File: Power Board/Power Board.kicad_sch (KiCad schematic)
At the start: 0 parts

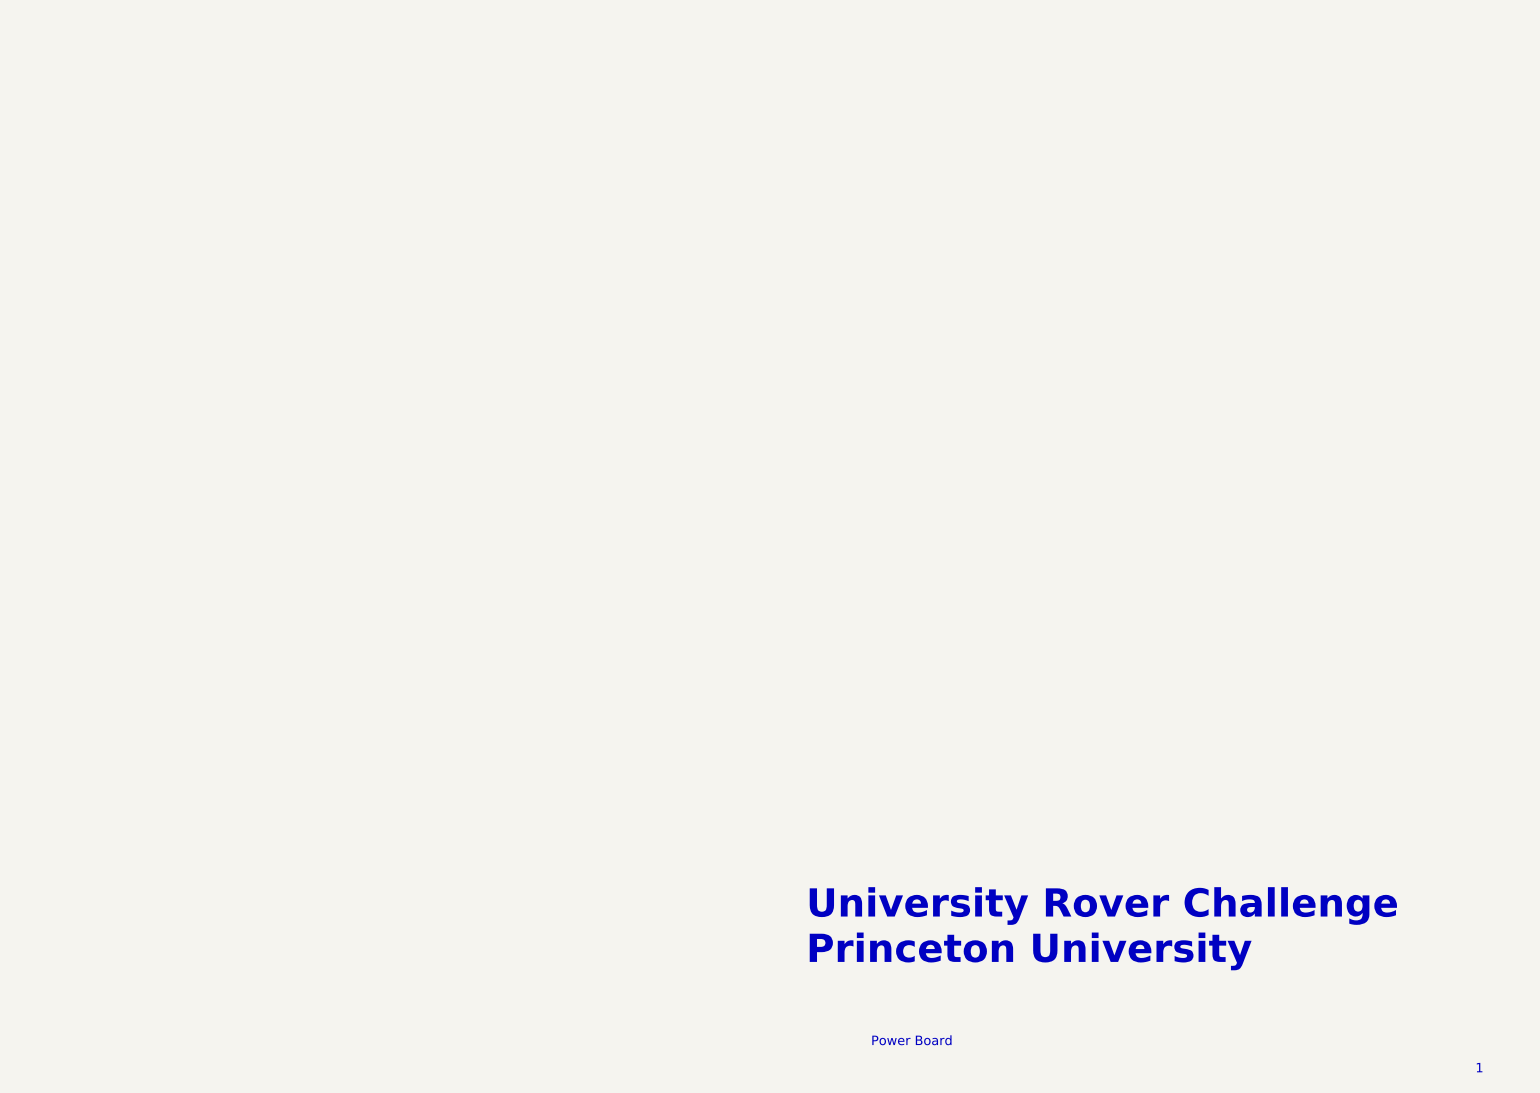
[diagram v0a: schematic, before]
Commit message: Updated power board schematic and libraries
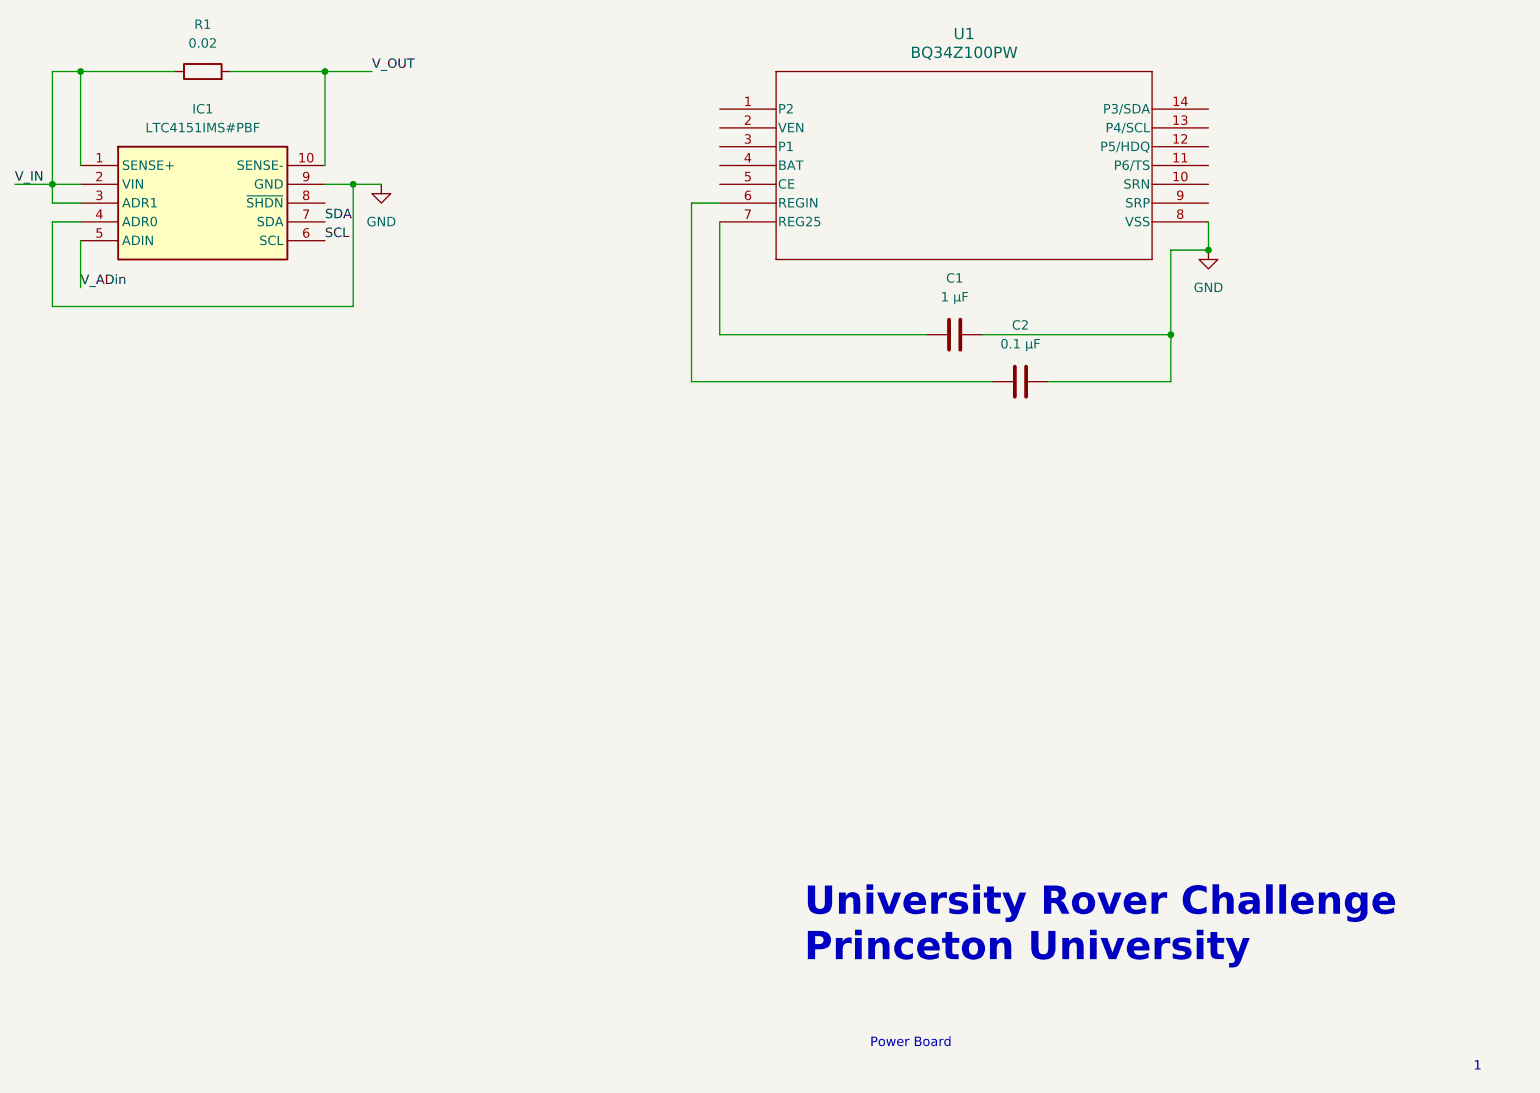
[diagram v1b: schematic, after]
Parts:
- added C1: 1 μF, symbol Device:C
- added C2: 0.1 μF, symbol Device:C
- added IC1: LTC4151IMS#PBF, SOP50P490X110-10N, symbol LTC4151IMS#PBF:LTC4151IMS#PBF
- added R1: 0.02, symbol Device:R
- added U1: BQ34Z100PW, PW14_TEX, symbol BQ34Z100PW:BQ34Z100PW
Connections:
- new net: C2.1, U1.6 (REGIN)
- new net: C1.1, U1.7 (REG25)
- new net GND: C1.2, C2.2, IC1.4 (ADR0), IC1.9 (GND), U1.8 (VSS)
- new net SCL: IC1.6 (SCL)
- new net SDA: IC1.7 (SDA)
- new net V_ADin: IC1.5 (ADIN)
- new net V_IN: IC1.1 (SENSE+), IC1.2 (VIN), IC1.3 (ADR1), R1.1
- new net V_OUT: IC1.10 (SENSE-), R1.2

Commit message: Worked on gas gauge
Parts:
- added R2, R3, R4: R, symbol Device:R
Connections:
- net GND: now also U1.1 (P2), U1.12 (P5/HDQ), U1.3 (P1)
- net SCL: now also U1.13 (P4/SCL)
- net SDA: now also U1.14 (P3/SDA)
- net PACK-: now reaches U1.10 (SRN)
- net PACK-: now also R2.1
- net at U1.4 (BAT): now also R3.2, R4.1
- net BAT-: now reaches U1.9 (SRP)
- net BAT-: now also R2.2
- new net BAT+: R3.1
- new net GNDA: R4.2
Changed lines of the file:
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@@
   (junction (at 76.2 73.66) (diameter 0) (color 0 0 0 0)
   )
+  (junction (at 232.41 78.74) (diameter 0) (color 0 0 0 0)
+  )
+  (junction (at 148.59 78.74) (diameter 0) (color 0 0 0 0)
+  )
+  (junction (at 160.02 63.5) (diameter 0) (color 0 0 0 0)
+  )
   (junction (at 116.84 73.66) (diameter 0) (color 0 0 0 0)
   )
   (junction (at 227.33 93.98) (diameter 0) (color 0 0 0 0)
   )
+  (junction (at 240.03 73.66) (diameter 0) (color 0 0 0 0)
+  )
   (junction (at 232.41 82.55) (diameter 0) (color 0 0 0 0)
   )
   (junction (at 113.03 58.42) (diameter 0) (color 0 0 0 0)
   )
+  (wire (pts (xy 80.01 58.42) (xy 92.71 58.42))
+    (stroke (width 0) (type default))
+  )
+  (wire (pts (xy 160.02 63.5) (xy 166.37 63.5))
+    (stroke (width 0) (type default))
+  )
+  (wire (pts (xy 233.68 81.28) (xy 240.03 81.28))
+    (stroke (width 0) (type default))
+  )
+  (wire (pts (xy 80.01 81.28) (xy 80.01 87.63))
+    (stroke (width 0) (type default))
+  )
+  (wire (pts (xy 233.68 81.28) (xy 233.68 76.2))
+    (stroke (width 0) (type default))
+  )
+  (wire (pts (xy 148.59 86.36) (xy 148.59 90.17))
+    (stroke (width 0) (type default))
+  )
+  (wire (pts (xy 237.49 68.58) (xy 237.49 78.74))
+    (stroke (width 0) (type default))
+  )
+  (wire (pts (xy 232.41 73.66) (xy 240.03 73.66))
+    (stroke (width 0) (type default))
+  )
+  (wire (pts (xy 240.03 73.66) (xy 248.92 73.66))
+    (stroke (width 0) (type default))
+  )
+  (wire (pts (xy 116.84 73.66) (xy 116.84 90.17))
+    (stroke (width 0) (type default))
+  )
+  (wire (pts (xy 227.33 82.55) (xy 232.41 82.55))
+    (stroke (width 0) (type default))
+  )
+  (wire (pts (xy 154.94 63.5) (xy 160.02 63.5))
+    (stroke (width 0) (type default))
+  )
+  (wire (pts (xy 76.2 78.74) (xy 76.2 90.17))
+    (stroke (width 0) (type default))
+  )
+  (wire (pts (xy 227.33 93.98) (xy 227.33 82.55))
+    (stroke (width 0) (type default))
+  )
+  (wire (pts (xy 142.24 69.85) (xy 148.59 69.85))
+    (stroke (width 0) (type default))
+  )
+  (wire (pts (xy 166.37 76.2) (xy 162.56 76.2))
+    (stroke (width 0) (type default))
+  )
+  (wire (pts (xy 113.03 58.42) (xy 119.38 58.42))
+    (stroke (width 0) (type default))
+  )
+  (wire (pts (xy 232.41 63.5) (xy 241.3 63.5))
+    (stroke (width 0) (type default))
+  )
   (wire (pts (xy 232.41 78.74) (xy 232.41 82.55))
     (stroke (width 0) (type default))
   )
-  (wire (pts (xy 80.01 58.42) (xy 92.71 58.42))
-    (stroke (width 0) (type default))
-  )
-  (wire (pts (xy 80.01 81.28) (xy 80.01 87.63))
-    (stroke (width 0) (type default))
-  )
-  (wire (pts (xy 116.84 73.66) (xy 116.84 90.17))
-    (stroke (width 0) (type default))
-  )
-  (wire (pts (xy 227.33 82.55) (xy 232.41 82.55))
-    (stroke (width 0) (type default))
-  )
-  (wire (pts (xy 76.2 78.74) (xy 76.2 90.17))
-    (stroke (width 0) (type default))
-  )
-  (wire (pts (xy 227.33 93.98) (xy 227.33 82.55))
-    (stroke (width 0) (type default))
-  )
-  (wire (pts (xy 166.37 76.2) (xy 162.56 76.2))
-    (stroke (width 0) (type default))
-  )
-  (wire (pts (xy 113.03 58.42) (xy 119.38 58.42))
-    (stroke (width 0) (type default))
-  )
   (wire (pts (xy 210.82 100.33) (xy 227.33 100.33))
     (stroke (width 0) (type default))
@@
     (stroke (width 0) (type default))
   )
+  (wire (pts (xy 148.59 83.82) (xy 148.59 78.74))
+    (stroke (width 0) (type default))
+  )
+  (wire (pts (xy 156.21 78.74) (xy 148.59 78.74))
+    (stroke (width 0) (type default))
+  )
+  (wire (pts (xy 233.68 76.2) (xy 232.41 76.2))
+    (stroke (width 0) (type default))
+  )
+  (wire (pts (xy 148.59 77.47) (xy 148.59 78.74))
+    (stroke (width 0) (type default))
+  )
   (wire (pts (xy 76.2 73.66) (xy 76.2 58.42))
     (stroke (width 0) (type default))
   )
+  (wire (pts (xy 166.37 71.12) (xy 156.21 71.12))
+    (stroke (width 0) (type default))
+  )
+  (wire (pts (xy 232.41 66.04) (xy 241.3 66.04))
+    (stroke (width 0) (type default))
+  )
   (wire (pts (xy 227.33 100.33) (xy 227.33 93.98))
     (stroke (width 0) (type default))
@@
     (stroke (width 0) (type default))
   )
+  (wire (pts (xy 166.37 68.58) (xy 160.02 68.58))
+    (stroke (width 0) (type default))
+  )
   (wire (pts (xy 162.56 76.2) (xy 162.56 100.33))
     (stroke (width 0) (type default))
   )
+  (wire (pts (xy 160.02 68.58) (xy 160.02 63.5))
+    (stroke (width 0) (type default))
+  )
   (wire (pts (xy 80.01 78.74) (xy 76.2 78.74))
     (stroke (width 0) (type default))
   )
+  (wire (pts (xy 156.21 71.12) (xy 156.21 78.74))
+    (stroke (width 0) (type default))
+  )
   (wire (pts (xy 76.2 90.17) (xy 116.84 90.17))
+    (stroke (width 0) (type default))
+  )
+  (wire (pts (xy 232.41 68.58) (xy 237.49 68.58))
+    (stroke (width 0) (type default))
+  )
+  (wire (pts (xy 237.49 78.74) (xy 232.41 78.74))
     (stroke (width 0) (type default))
   )
@@
     (effects (font (size 1.27 1.27)) (justify left bottom))
   )
+  (label "SDA" (at 234.95 63.5 0) (fields_autoplaced)
+    (effects (font (size 1.27 1.27)) (justify left bottom))
+  )
+  (label "SCL" (at 234.95 66.04 0) (fields_autoplaced)
+    (effects (font (size 1.27 1.27)) (justify left bottom))
+  )
   (label "V_OUT" (at 119.38 58.42 0) (fields_autoplaced)
     (effects (font (size 1.27 1.27)) (justify left bottom))
   )
+  (label "BAT-" (at 233.68 81.28 0) (fields_autoplaced)
+    (effects (font (size 1.27 1.27)) (justify left bottom))
+  )
   (label "V_ADin" (at 80.01 87.63 0) (fields_autoplaced)
     (effects (font (size 1.27 1.27)) (justify left bottom))
   )
+  (label "BAT+" (at 143.51 69.85 0) (fields_autoplaced)
+    (effects (font (size 1.27 1.27)) (justify left bottom))
+  )
+  (label "PACK-" (at 242.57 73.66 0) (fields_autoplaced)
+    (effects (font (size 1.27 1.27)) (justify left bottom))
+  )
   (label "SDA" (at 113.03 78.74 0) (fields_autoplaced)
     (effects (font (size 1.27 1.27)) (justify left bottom))
@@
   (label "V_IN" (at 71.12 73.66 0) (fields_autoplaced)
     (effects (font (size 1.27 1.27)) (justify left bottom))
+  )
+  (symbol (lib_id "power:GND") (at 154.94 63.5 0) (unit 1)
+    (in_bom yes) (on_board yes) (dnp no) (fields_autoplaced)
+    (property "Reference" "#PWR03" (at 154.94 69.85 0)
+      (effects (font (size 1.27 1.27)) hide)
+    )
+    (property "Value" "GND" (at 154.94 68.58 0)
+      (effects (font (size 1.27 1.27)))
+    )
+    (property "Footprint" "" (at 154.94 63.5 0)
+      (effects (font (size 1.27 1.27)) hide)
+    )
+    (property "Datasheet" "" (at 154.94 63.5 0)
+      (effects (font (size 1.27 1.27)) hide)
+    )
+    (pin "1")
+    (instances
+      (project "Power Board"
+        (path "/52f7cba9-f573-43e9-b6c5-44859a4c1733"
+          (reference "#PWR03") (unit 1)
+        )
+      )
+    )
+  )
+  (symbol (lib_id "power:GNDA") (at 148.59 90.17 0) (unit 1)
+    (in_bom yes) (on_board yes) (dnp no) (fields_autoplaced)
+    (property "Reference" "#PWR04" (at 148.59 96.52 0)
+      (effects (font (size 1.27 1.27)) hide)
+    )
+    (property "Value" "GNDA" (at 148.59 95.25 0)
+      (effects (font (size 1.27 1.27)))
+    )
+    (property "Footprint" "" (at 148.59 90.17 0)
+      (effects (font (size 1.27 1.27)) hide)
+    )
+    (property "Datasheet" "" (at 148.59 90.17 0)
+      (effects (font (size 1.27 1.27)) hide)
+    )
+    (pin "1")
+    (instances
+      (project "Power Board"
+        (path "/52f7cba9-f573-43e9-b6c5-44859a4c1733"
+          (reference "#PWR04") (unit 1)
+        )
+      )
+    )
   )
   (symbol (lib_id "BQ34Z100PW:BQ34Z100PW") (at 166.37 63.5 0) (unit 1)
@@
         )
       )
+    )
+  )
+  (symbol (lib_id "Device:R") (at 148.59 82.55 0) (unit 1)
+    (in_bom yes) (on_board yes) (dnp no) (fields_autoplaced)
+    (property "Reference" "R4" (at 151.13 81.28 0)
+      (effects (font (size 1.27 1.27)) (justify left))
+    )
+    (property "Value" "R" (at 151.13 83.82 0)
+      (effects (font (size 1.27 1.27)) (justify left))
+    )
+    (property "Footprint" "" (at 146.812 82.55 90)
+      (effects (font (size 1.27 1.27)) hide)
+    )
+    (property "Datasheet" "~" (at 148.59 82.55 0)
+      (effects (font (size 1.27 1.27)) hide)
+    )
+    (pin "1")
+    (pin "2")
+    (instances
+      (project "Power Board"
+        (path "/52f7cba9-f573-43e9-b6c5-44859a4c1733"
+          (reference "R4") (unit 1)
+        )
+      )
+    )
+  )
+  (symbol (lib_id "Device:R") (at 148.59 73.66 0) (unit 1)
+    (in_bom yes) (on_board yes) (dnp no) (fields_autoplaced)
+    (property "Reference" "R3" (at 151.13 72.39 0)
+      (effects (font (size 1.27 1.27)) (justify left))
+    )
+    (property "Value" "R" (at 151.13 74.93 0)
+      (effects (font (size 1.27 1.27)) (justify left))
+    )
+    (property "Footprint" "" (at 146.812 73.66 90)
+      (effects (font (size 1.27 1.27)) hide)
+    )
+    (property "Datasheet" "~" (at 148.59 73.66 0)
+      (effects (font (size 1.27 1.27)) hide)
+    )
+    (pin "1")
+    (pin "2")
+    (instances
+      (project "Power Board"
+        (path "/52f7cba9-f573-43e9-b6c5-44859a4c1733"
+          (reference "R3") (unit 1)
+        )
+      )
+    )
+  )
+  (symbol (lib_id "Device:R") (at 240.03 77.47 0) (unit 1)
+    (in_bom yes) (on_board yes) (dnp no) (fields_autoplaced)
+    (property "Reference" "R2" (at 242.57 76.2 0)
+      (effects (font (size 1.27 1.27)) (justify left))
+    )
+    (property "Value" "R" (at 242.57 78.74 0)
+      (effects (font (size 1.27 1.27)) (justify left))
+    )
+    (property "Footprint" "" (at 238.252 77.47 90)
+      (effects (font (size 1.27 1.27)) hide)
+    )
+    (property "Datasheet" "~" (at 240.03 77.47 0)
+      (effects (font (size 1.27 1.27)) hide)
+    )
+    (pin "1")
+    (pin "2")
+    (instances
+      (project "Power Board"
+        (path "/52f7cba9-f573-43e9-b6c5-44859a4c1733"
+          (reference "R2") (unit 1)
+        )
+      )
